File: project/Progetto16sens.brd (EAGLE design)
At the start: 228.6 x 231.1 mm, 148 parts, among them IC1 LMZ14202TZE-ADJ_NOPB, J2 455-1750-1-ND, M1 43650-0201, M2 43650-0201, M3 43650-0201, M4 43650-0201, M5 ARDUINO-PRO-MINI, SW1 TL32PO, SW2 TL32PO, SW3 TL32PO

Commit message: continuing brd
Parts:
- moved CB1 129.3 mm to (-55.8, 79.2)
- moved RB1 129.2 mm to (-55.7, 76.9), turned to 180 degrees
- moved CB3 100.4 mm to (50.9, -82.3), turned to 180 degrees
- moved RB3 100.4 mm to (50.9, -80.0)
- moved CB2 91.5 mm to (-56.0, -79.4), turned to 0 degrees
- moved RB2 91.4 mm to (-56.0, -77.1)
- moved LED1 15.3 mm to (62.2, -22.9), turned to 180 degrees
- moved R24 12.7 mm to (52.1, -16.5), flipped to the bottom, turned to 90 degrees
- moved R26 10.5 mm to (62.2, -16.5), flipped to the bottom, turned to 90 degrees
- moved R25 9.16 mm to (57.1, -16.5), flipped to the bottom, turned to 90 degrees
- moved ROLL 8.03 mm to (-62.2, -41.9)
- moved RB4 6.48 mm to (44.5, 81.4)
- moved CB4 6.30 mm to (46.7, 81.4), turned to 270 degrees
- moved LED2 5.24 mm to (57.1, -22.9), turned to 180 degrees
- moved LED3 5.24 mm to (52.1, -22.9), turned to 180 degrees
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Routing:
- net GND: track 110.0 -> 130.8 mm, vias 2 -> 14
- net PWR_B3: track 0.00 -> 20.6 mm
- net PWR_B1: track 0.00 -> 19.6 mm
- net PWR_B2: track 0.00 -> 18.9 mm
- net PWR_B4: track 0.00 -> 10.3 mm
- added copper zone on layer 1, net GND
- added copper zone on layer 1, net PWR_B1
- added copper zone on layer 1, net PWR_B2
- added copper zone on layer 1, net PWR_B3
- added copper zone on layer 1, net PWR_B4

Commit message: continuing brd
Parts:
- moved R13 7.28 mm to (-49.3, 24.5), turned to 180 degrees
- moved R12 5.80 mm to (-78.4, -4.60), turned to 180 degrees
- moved R10 5.76 mm to (-48.5, -4.60), turned to 180 degrees
- moved R20 5.56 mm to (-78.4, -2.31), turned to 180 degrees
- moved R9 5.52 mm to (-48.5, -2.31), turned to 180 degrees
- moved R7 5.06 mm to (-69.9, 44.1), turned to 0 degrees
- moved R17 3.09 mm to (-62.0, -5.81)
- moved R8 2.94 mm to (-49.3, 31.8)
- moved R16 2.88 mm to (-49.3, 29.4)
- moved R14 2.59 mm to (-49.3, 26.8), turned to 180 degrees
- moved M2- 2.13 mm to (-55.4, 35.6)
- moved M1+ 2.13 mm to (-68.6, 37.9)
- moved M1- 2.13 mm to (-68.6, 35.8)
- moved M2+ 2.13 mm to (-55.4, 37.9)
- moved R19 2.01 mm to (-68.5, -22.8)
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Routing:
- net GND: track 130.8 -> 172.9 mm
- net N$24: track 0.00 -> 30.6 mm, vias 0 -> 2
- net N$25: track 0.00 -> 29.7 mm, vias 0 -> 2
- net N$36: track 0.00 -> 29.3 mm, vias 0 -> 2
- net N$26: track 0.00 -> 27.7 mm, vias 0 -> 2
- net N$28: track 0.00 -> 27.6 mm, vias 0 -> 2
- net N$34: track 0.00 -> 18.6 mm, vias 0 -> 2
- net N$33: track 0.00 -> 16.2 mm, vias 0 -> 2
- net M4_INB: track 11.9 -> 22.5 mm
- net N$22: track 0.00 -> 1.79 mm, vias 0 -> 1
- net PWR_B2: track 18.9 -> 19.4 mm
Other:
- outline, holes or cut-outs redrawn

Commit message: continuing brd
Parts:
- moved C20 8.20 mm to (46.5, 77.6), flipped to the bottom, turned to 180 degrees
- moved R11 2.54 mm to (-59.6, -22.8)
- moved R14 2.54 mm to (-49.3, 24.3)
- moved R19 2.54 mm to (-71.0, -22.8)
- moved R13 2.03 mm to (-49.3, 26.6)
- moved R15 1.53 mm to (-58.3, 43.9)
- moved R7 1.53 mm to (-71.5, 43.9)
- moved R8 0.64 mm to (-49.3, 31.1)
- moved R16 0.51 mm to (-49.3, 28.9)
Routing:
- net GND: track 172.9 -> 100.0 mm
- net A_RX: track 53.4 -> 0.16 mm, vias 1 -> 0
- net A_TX: track 53.2 -> 0.16 mm, vias 1 -> 0
- net N$32: track 0.00 -> 33.6 mm, vias 0 -> 2
- net N$30: track 0.00 -> 29.3 mm, vias 0 -> 2
- net N$29: track 0.00 -> 26.9 mm, vias 0 -> 2
- net B1: track 24.8 -> 0.51 mm
- net +3V3: track 60.1 -> 40.7 mm
- net N$116: track 19.4 -> 0.00 mm
- net N$22: track 1.79 -> 19.9 mm, vias 1 -> 2
- net N$23: track 0.00 -> 17.0 mm, vias 0 -> 2
- net N$117: track 15.9 -> 0.00 mm
- net N$27: track 0.00 -> 13.8 mm
- net N$35: track 0.00 -> 13.0 mm
- net N$21: track 0.00 -> 12.1 mm
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
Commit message: continuing brd
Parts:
- moved U$3 26.5 mm to (14.1, -9.50), flipped to the bottom
- moved LS_N 3.81 mm to (-16.9, 78.3)
- moved LS_E 2.54 mm to (-2.92, 78.3)
- moved BALL_MUX 1.27 mm to (42.8, 46.5)
- moved R_BALL 1.27 mm to (54.2, 52.9)
- moved LS_S 1.27 mm to (11.0, 78.3)
- moved L_BALL 1.27 mm to (58.0, 52.9)
- moved SW_BALL 1.27 mm to (55.5, 44.0)
- moved C19 0.89 mm to (2.54, -5.11), turned to 180 degrees
- moved R21 0.89 mm to (2.54, -0.48)
- moved R22 0.89 mm to (2.54, -2.77)
- moved C10 0.65 mm to (34.0, -10.0)
- turned SW1 to 90 degrees
- turned SW2 to 90 degrees
- turned SW3 to 90 degrees
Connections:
- removed net N$13: L_SW2.A, R_SW2.1
- removed net N$15: R_SW2.2, SW2.3
- removed net N$16: L_SW3.A, R_SW3.1
- removed net N$17: R_SW3.2, SW3.3
- removed net N$5: L_SW1.A, R_SW1.1
- removed net N$8: R_SW1.2, SW1.3
- removed net N$81: J1.6, M5.J6.4
- new net N$1: L_SW2.C, R_SW2.2
- new net N$2: L_SW1.C, R_SW1.2
- new net N$3: L_SW3.C, R_SW3.2
- net +3V3: now also J1.6, M5.J6.4, SW1.3, SW2.3, SW3.3; no longer L_SW1.C, L_SW2.C, L_SW3.C
- net GND: now also R_SW1.1, R_SW2.1, R_SW3.1
- net SW1: now also L_SW1.A
- net SW2: now also L_SW2.A
- net SW3: now also L_SW3.A
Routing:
- net +3V3: track 40.7 -> 257.1 mm
- net K_DIG: track 0.16 -> 210.0 mm
- net R_DIG: track 0.16 -> 192.9 mm
- net K_PWM: track 0.00 -> 180.8 mm, vias 0 -> 1
- net R_PWM: track 0.00 -> 164.2 mm, vias 0 -> 1
- net M1_INA: track 0.16 -> 68.8 mm
- net M2_INB: track 0.16 -> 68.8 mm, vias 0 -> 2
- net M1_INB: track 0.16 -> 68.2 mm, vias 0 -> 2
- net M2_INA: track 0.16 -> 67.6 mm, vias 0 -> 2
- net M1_PWM: track 0.16 -> 48.2 mm
- net SCL: track 0.16 -> 46.2 mm, vias 0 -> 1
- net M2_PWM: track 0.16 -> 44.9 mm
- net SDA: track 0.16 -> 43.8 mm, vias 0 -> 1
- net GND: track 100.0 -> 103.2 mm

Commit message: halfway done with wiring SEE WIRESTUB ERROR
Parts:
- moved CB2 4.31 mm to (-59.3, -77.6)
- moved RB2 4.31 mm to (-59.3, -75.3)
- moved J1 3.81 mm to (83.4, 27.5)
- moved J2 3.81 mm to (83.4, -13.2)
- moved LS_N 2.84 mm to (-18.2, 80.8), turned to 180 degrees
- moved LS_E 2.84 mm to (-4.19, 80.8), turned to 180 degrees
- moved LS_S 2.84 mm to (9.78, 80.8), turned to 180 degrees
- moved LS_W 2.84 mm to (23.7, 80.8), turned to 180 degrees
- moved C20 2.54 mm to (46.5, 80.1)
- moved RB4 2.54 mm to (45.3, 84.7)
- moved CB4 2.54 mm to (47.6, 84.8)
- moved L_BALL 1.25 mm to (56.9, 52.4)
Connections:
- removed net N$116: J2.2, M5.J3.2
- removed net N$117: J2.3, M5.J3.3
- removed net N$61: R_BALL.2, SW_BALL.1
- new net BX: J1.11, M5.J6.9
- net B1: now also BALL_MUX.2, J2.3, M5.J3.3; no longer BALL_MUX.9, J1.1, M5.J2.2
- net B10: now also BALL_MUX.17, M5.J7.8, SV4.8; no longer BALL_MUX.22, M5.J7.1, SV4.1
- net B11: now also BALL_MUX.18, J1.10, M5.J6.8; no longer BALL_MUX.21
- net B12: now also BALL_MUX.19, J1.9, M5.J6.7; no longer BALL_MUX.20, J1.7, M5.J6.5
- net B13: now also BALL_MUX.20; no longer BALL_MUX.19
- net B14: now also BALL_MUX.21, J1.7, M5.J6.5; no longer BALL_MUX.18, J1.9, M5.J6.7
- net B15: now also BALL_MUX.22, J1.1, M5.J2.2; no longer BALL_MUX.17, J1.10, M5.J6.8
- net B16: now also BALL_MUX.23, J1.2, M5.J2.1; no longer BALL_MUX.16, J1.11, M5.J6.9
- net B2: now also BALL_MUX.3, J2.2, M5.J3.2; no longer BALL_MUX.8, J1.2, M5.J2.1
- net B3: now also BALL_MUX.4, M5.J7.1, SV4.1; no longer BALL_MUX.7, M5.J7.8, SV4.8
- net B4: now also BALL_MUX.5, M5.J7.2, SV4.2; no longer BALL_MUX.6, M5.J7.7, SV4.7
- net B5: now also BALL_MUX.6, M5.J7.3, SV4.3; no longer BALL_MUX.5, M5.J7.6, SV4.6
- net B6: now also BALL_MUX.7, M5.J7.4, SV4.4; no longer BALL_MUX.4, M5.J7.5, SV4.5
- net B7: now also BALL_MUX.8, M5.J7.5, SV4.5; no longer BALL_MUX.3, M5.J7.4, SV4.4
- net B8: now also BALL_MUX.9, M5.J7.6, SV4.6; no longer BALL_MUX.2, M5.J7.3, SV4.3
- net B9: now also BALL_MUX.16, M5.J7.7, SV4.7; no longer BALL_MUX.23, M5.J7.2, SV4.2
- net E_IN: now also SV6.3, U$1.17/A3/TX4/SDA1; no longer SV6.2, U$1.16/A2/RX4/SCL1
- net E_OUT: now also SV6.2, U$1.16/A2/RX4/SCL1; no longer SV6.3, U$1.17/A3/TX4/SDA1
- net N_IN: now also SV6.5, U$1.19/A5/SCL; no longer SV6.4, U$1.18/A4/SDA
- net N_OUT: now also SV6.4, U$1.18/A4/SDA; no longer SV6.5, U$1.19/A5/SCL
- net S_IN: now also SV6.1, U$1.15/A1/RX3; no longer SV3.12, U$1.14/A0/TX3
- net S_OUT: now also SV3.12, U$1.14/A0/TX3; no longer SV6.1, U$1.15/A1/RX3
- net W_IN: now also SV3.9, U$1.41/A17; no longer SV3.8, U$1.40/A16
- net W_OUT: now also SV3.8, U$1.40/A16; no longer SV3.9, U$1.41/A17
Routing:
- net B8: track 0.00 -> 729.1 mm
- net B9: track 0.00 -> 692.7 mm
- net B10: track 0.66 -> 687.4 mm
- net B7: track 0.00 -> 664.0 mm
- net B6: track 0.00 -> 592.2 mm
- net B5: track 0.00 -> 524.0 mm
- net B4: track 0.00 -> 449.2 mm
- net B3: track 0.00 -> 385.5 mm
- net B2: track 0.00 -> 305.8 mm
- net B11: track 0.00 -> 281.9 mm
- net B1: track 0.51 -> 238.3 mm
- net B12: track 0.00 -> 214.5 mm
- net K_DIG: track 210.0 -> 1.86 mm
- net R_DIG: track 192.9 -> 0.00 mm
- net K_PWM: track 180.8 -> 1.27 mm, vias 1 -> 0
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
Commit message: halfway done with wiring SEE WIRESTUB ERROR
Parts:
- moved LED1 67.9 mm to (-4.19, -31.0)
- moved LED2 67.9 mm to (-9.27, -31.0)
- moved LED3 67.9 mm to (-14.4, -31.0)
- moved R24 67.9 mm to (-14.4, -24.6)
- moved R25 67.9 mm to (-9.27, -24.6)
- moved R26 67.9 mm to (-4.19, -24.6)
- moved L_SW1 13.3 mm to (51.7, -34.8)
- moved L_SW3 13.3 mm to (72.0, -34.8)
- moved R_SW1 13.3 mm to (51.7, -34.8)
- moved R_SW3 13.3 mm to (72.0, -34.8)
- moved L_SW2 13.3 mm to (61.8, -34.8)
- moved R_SW2 13.3 mm to (61.8, -34.8)
- moved SW1 13.3 mm to (51.7, -24.6)
- moved SW3 13.3 mm to (72.0, -24.6)
- moved SW2 13.3 mm to (61.8, -24.6)
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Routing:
- net K_DIG: track 1.86 -> 135.2 mm, vias 0 -> 2
- net R_DIG: track 0.00 -> 127.1 mm, vias 0 -> 2
- net BT_TX: track 0.00 -> 82.3 mm
- net BT_RX: track 0.00 -> 78.0 mm
- net BUZZ: track 0.00 -> 44.8 mm, vias 0 -> 2
- net +3V3: track 253.7 -> 219.4 mm
- net A_RX: track 0.00 -> 34.2 mm, vias 0 -> 2
- net A_TX: track 0.00 -> 33.9 mm
- net B4: track 449.2 -> 445.1 mm
- net B5: track 524.0 -> 519.9 mm
- net B7: track 664.0 -> 659.9 mm
- net B6: track 592.2 -> 588.1 mm
- net B8: track 729.1 -> 725.0 mm
- net B3: track 385.5 -> 388.4 mm
- net K_PWM: track 1.27 -> 0.00 mm
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
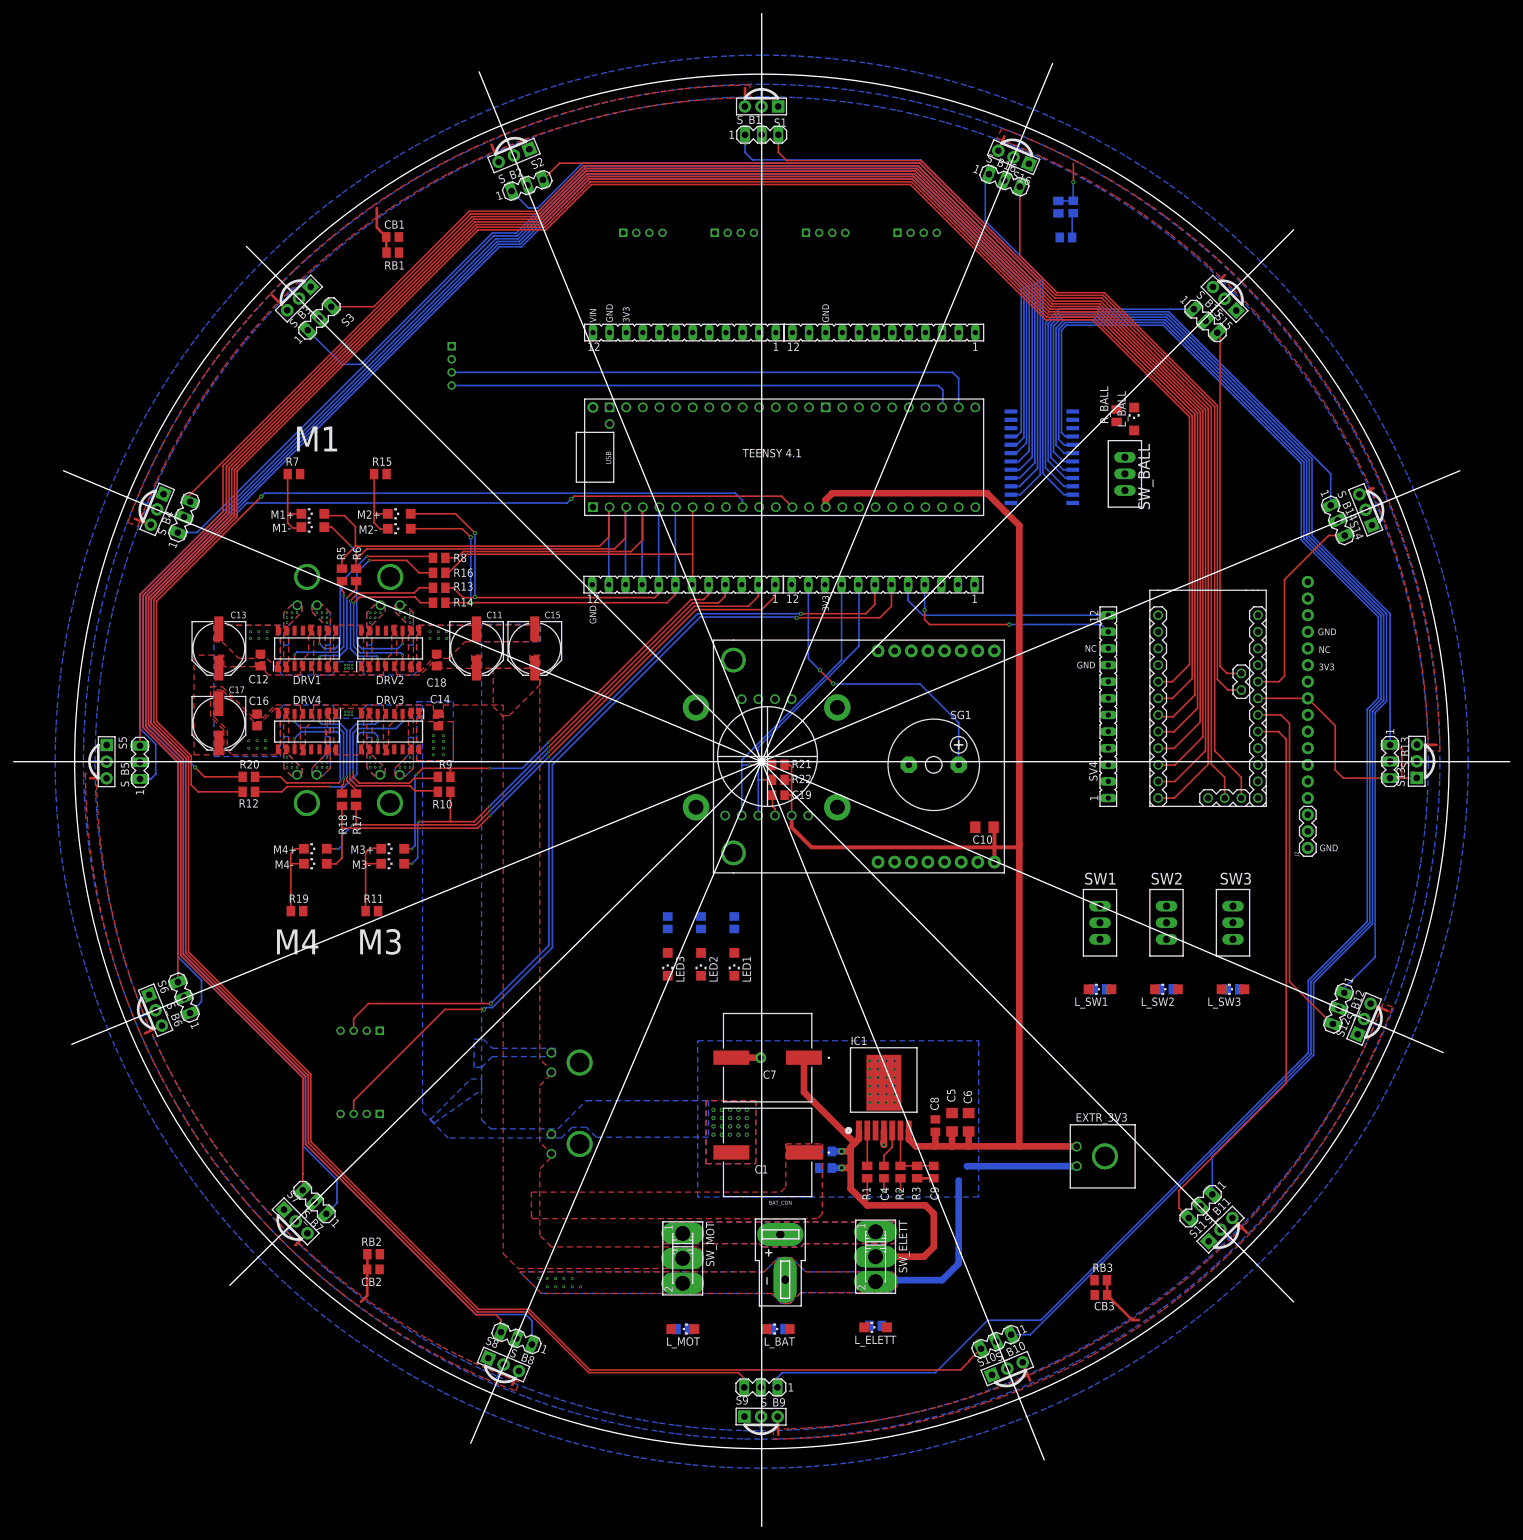
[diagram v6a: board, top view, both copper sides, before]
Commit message: elaborato almost done, board needs some fixing
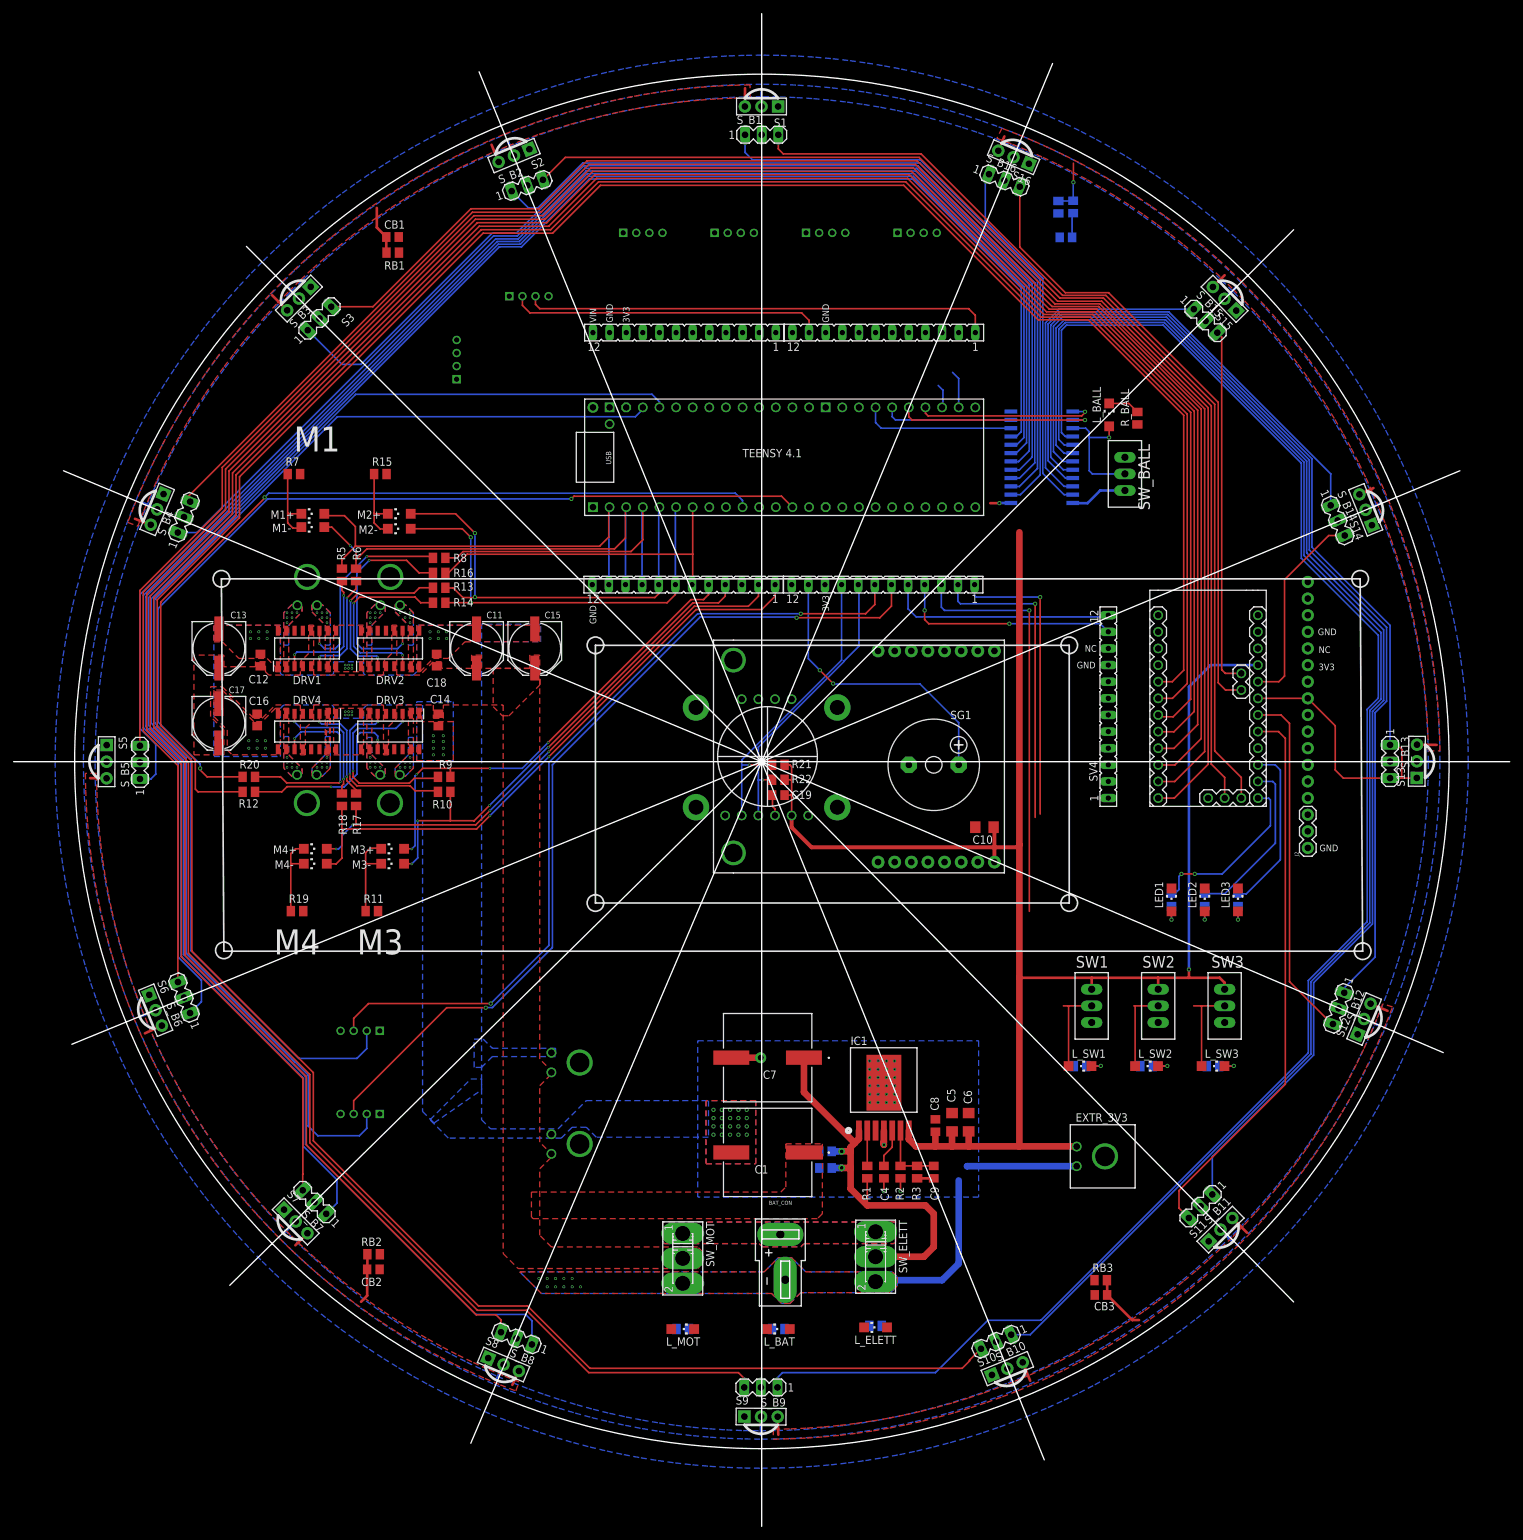
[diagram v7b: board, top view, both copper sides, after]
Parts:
- added BALL_TAKE: 4P-2.0, OPL_Connector:HW4-2.0
- moved LED3 87.7 mm to (72.8, -21.1), turned to 0 degrees
- moved R24 87.2 mm to (72.8, -21.1), turned to 270 degrees
- moved LED2 77.6 mm to (67.7, -21.1), turned to 0 degrees
- moved R25 77.0 mm to (67.7, -21.1), turned to 270 degrees
- moved LED1 67.5 mm to (62.6, -21.1), turned to 0 degrees
- moved R26 66.9 mm to (62.6, -21.1), turned to 270 degrees
- moved SW1 12.8 mm to (50.4, -37.3)
- moved SW2 12.8 mm to (60.6, -37.3)
- moved SW3 12.8 mm to (70.7, -37.3)
- moved L_SW1 12.1 mm to (48.6, -46.5), turned to 270 degrees
- moved L_SW3 12.1 mm to (69.0, -46.5), turned to 270 degrees
- moved R_SW1 12.1 mm to (48.6, -46.5), turned to 180 degrees
- moved R_SW3 12.1 mm to (69.0, -46.5), turned to 180 degrees
- moved L_SW2 12.1 mm to (58.8, -46.5), turned to 270 degrees
- moved R_SW2 12.1 mm to (58.8, -46.5), turned to 180 degrees
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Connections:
- net BX renamed LED4
- removed net N$60: BALL_MUX.15, SW_BALL.2
- removed net N$62: L_BALL.A, R_BALL.1
- new net ENABLE: BALL_MUX.15, L_BALL.A, SW_BALL.2
- new net N$8: L_BALL.C, R_BALL.2
- net +3V3: now also BALL_TAKE.1
- net BALL_IN: now also BALL_TAKE.2
- net BALL_OUT: now also BALL_TAKE.3
- net GND: now also BALL_TAKE.4, R_BALL.1, SW_BALL.1; no longer L_BALL.C
- net LED1: now also J1.14, M5.J6.12; no longer J1.12, M5.J6.10
- net LED3: now also J1.12, M5.J6.10; no longer J1.14, M5.J6.12
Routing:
- net K_PWM: track 0.00 -> 195.4 mm
- net R_PWM: track 0.00 -> 179.9 mm
- net SW1: track 0.00 -> 76.6 mm, vias 0 -> 1
- net BT_TX: track 82.3 -> 5.74 mm
- net BT_RX: track 78.0 -> 3.70 mm
- net BALL_OUT: track 0.00 -> 71.8 mm
- net +3V3: track 219.4 -> 289.7 mm, vias 0 -> 2
- net SW2: track 0.00 -> 60.1 mm, vias 0 -> 1
- net SW3: track 0.00 -> 58.9 mm, vias 0 -> 1
- net BALL_IN: track 0.00 -> 48.0 mm
- net PWB_3: track 0.00 -> 30.5 mm, vias 0 -> 1
- net PWB_4: track 0.00 -> 27.7 mm, vias 0 -> 1
- net LED1: track 0.00 -> 26.6 mm, vias 0 -> 2
- net LED3: track 0.00 -> 26.1 mm
- net LED2: track 0.00 -> 25.9 mm
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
